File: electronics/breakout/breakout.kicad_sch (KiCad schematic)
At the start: 9 parts, among them J1 2604-3103, J2 2604-3103, J3 2604-3103, J4 2604-3103, J5 2604-3103, J6 2604-3103, J7 2604-3103, J8 2604-3105, J9 2604-3103

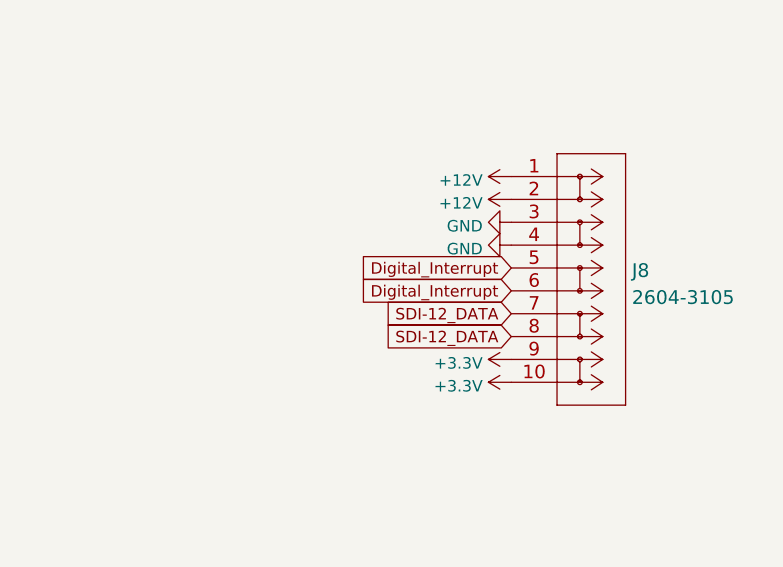
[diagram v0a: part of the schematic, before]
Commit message: Breakout board main connector now in same order as on the Wombat board.
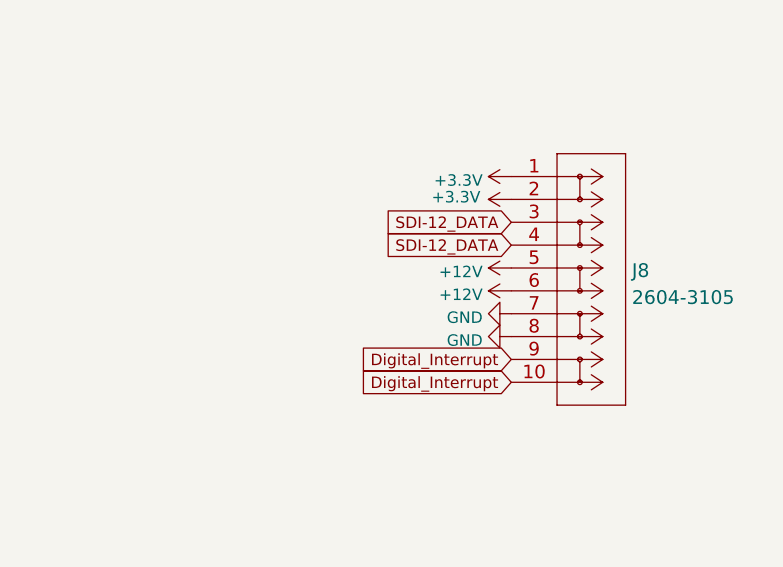
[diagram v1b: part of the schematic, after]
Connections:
- net +12V: now also J8.5, J8.6; no longer J8.1, J8.2
- net +3.3V: now also J8.1, J8.2; no longer J8.10, J8.9
- net Digital_Interrupt: now also J8.10, J8.9; no longer J8.5, J8.6
- net GND: now also J8.7, J8.8; no longer J8.3, J8.4
- net SDI-12_DATA: now also J8.3, J8.4; no longer J8.7, J8.8
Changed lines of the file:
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@@
     )
   )
-  (global_label "SDI-12_DATA" (shape input) (at 205.994 92.964 180) (fields_autoplaced)
-    (effects (font (size 1.27 1.27)) (justify right))
-    (property "Intersheet References" "${INTERSHEET_REFS}" (id 0) (at 191.1228 92.8846 0)
+  (global_label "SDI-12_DATA" (shape input) (at 205.994 82.804 180) (fields_autoplaced)
+    (effects (font (size 1.27 1.27)) (justify right))
+    (property "Intersheet References" "${INTERSHEET_REFS}" (id 0) (at 191.1228 82.7246 0)
       (effects (font (size 1.27 1.27)) (justify right) hide)
     )
@@
     )
   )
-  (global_label "Digital_Interrupt" (shape input) (at 205.994 85.344 180) (fields_autoplaced)
-    (effects (font (size 1.27 1.27)) (justify right))
-    (property "Intersheet References" "${INTERSHEET_REFS}" (id 0) (at 188.2804 85.2646 0)
+  (global_label "Digital_Interrupt" (shape input) (at 205.994 95.504 180) (fields_autoplaced)
+    (effects (font (size 1.27 1.27)) (justify right))
+    (property "Intersheet References" "${INTERSHEET_REFS}" (id 0) (at 188.2804 95.4246 0)
       (effects (font (size 1.27 1.27)) (justify right) hide)
     )
@@
     )
   )
-  (global_label "SDI-12_DATA" (shape input) (at 205.994 90.424 180) (fields_autoplaced)
-    (effects (font (size 1.27 1.27)) (justify right))
-    (property "Intersheet References" "${INTERSHEET_REFS}" (id 0) (at 191.1228 90.3446 0)
+  (global_label "SDI-12_DATA" (shape input) (at 205.994 80.264 180) (fields_autoplaced)
+    (effects (font (size 1.27 1.27)) (justify right))
+    (property "Intersheet References" "${INTERSHEET_REFS}" (id 0) (at 191.1228 80.1846 0)
       (effects (font (size 1.27 1.27)) (justify right) hide)
     )
@@
     )
   )
-  (global_label "Digital_Interrupt" (shape input) (at 205.994 87.884 180) (fields_autoplaced)
-    (effects (font (size 1.27 1.27)) (justify right))
-    (property "Intersheet References" "${INTERSHEET_REFS}" (id 0) (at 188.2804 87.8046 0)
+  (global_label "Digital_Interrupt" (shape input) (at 205.994 98.044 180) (fields_autoplaced)
+    (effects (font (size 1.27 1.27)) (justify right))
+    (property "Intersheet References" "${INTERSHEET_REFS}" (id 0) (at 188.2804 97.9646 0)
       (effects (font (size 1.27 1.27)) (justify right) hide)
     )
@@
     (pin "1")
   )
-  (symbol (lib_id "power:GND") (at 205.994 82.804 270) (unit 1)
-    (in_bom yes) (on_board yes) (fields_autoplaced)
-    (property "Reference" "#PWR032" (id 0) (at 199.644 82.804 0)
-      (effects (font (size 1.27 1.27)) hide)
-    )
-    (property "Value" "GND" (id 1) (at 202.8191 83.2378 90)
-      (effects (font (size 1.27 1.27)) (justify right))
-    )
-    (property "Footprint" "" (id 2) (at 205.994 82.804 0)
-      (effects (font (size 1.27 1.27)) hide)
-    )
-    (property "Datasheet" "" (id 3) (at 205.994 82.804 0)
+  (symbol (lib_id "power:GND") (at 205.994 92.964 270) (unit 1)
+    (in_bom yes) (on_board yes) (fields_autoplaced)
+    (property "Reference" "#PWR032" (id 0) (at 199.644 92.964 0)
+      (effects (font (size 1.27 1.27)) hide)
+    )
+    (property "Value" "GND" (id 1) (at 202.8191 93.3978 90)
+      (effects (font (size 1.27 1.27)) (justify right))
+    )
+    (property "Footprint" "" (id 2) (at 205.994 92.964 0)
+      (effects (font (size 1.27 1.27)) hide)
+    )
+    (property "Datasheet" "" (id 3) (at 205.994 92.964 0)
       (effects (font (size 1.27 1.27)) hide)
     )
@@
     (pin "1")
   )
-  (symbol (lib_id "power:GND") (at 205.994 80.264 270) (unit 1)
-    (in_bom yes) (on_board yes) (fields_autoplaced)
-    (property "Reference" "#PWR031" (id 0) (at 199.644 80.264 0)
-      (effects (font (size 1.27 1.27)) hide)
-    )
-    (property "Value" "GND" (id 1) (at 202.8191 80.6978 90)
-      (effects (font (size 1.27 1.27)) (justify right))
-    )
-    (property "Footprint" "" (id 2) (at 205.994 80.264 0)
-      (effects (font (size 1.27 1.27)) hide)
-    )
-    (property "Datasheet" "" (id 3) (at 205.994 80.264 0)
-      (effects (font (size 1.27 1.27)) hide)
-    )
-    (pin "1")
-  )
-  (symbol (lib_id "power:+3.3V") (at 205.994 98.044 90) (unit 1)
-    (in_bom yes) (on_board yes) (fields_autoplaced)
-    (property "Reference" "#PWR034" (id 0) (at 209.804 98.044 0)
-      (effects (font (size 1.27 1.27)) hide)
-    )
-    (property "Value" "+3.3V" (id 1) (at 202.819 98.4778 90)
-      (effects (font (size 1.27 1.27)) (justify left))
-    )
-    (property "Footprint" "" (id 2) (at 205.994 98.044 0)
-      (effects (font (size 1.27 1.27)) hide)
-    )
-    (property "Datasheet" "" (id 3) (at 205.994 98.044 0)
+  (symbol (lib_id "power:GND") (at 205.994 90.424 270) (unit 1)
+    (in_bom yes) (on_board yes) (fields_autoplaced)
+    (property "Reference" "#PWR031" (id 0) (at 199.644 90.424 0)
+      (effects (font (size 1.27 1.27)) hide)
+    )
+    (property "Value" "GND" (id 1) (at 202.8191 90.8578 90)
+      (effects (font (size 1.27 1.27)) (justify right))
+    )
+    (property "Footprint" "" (id 2) (at 205.994 90.424 0)
+      (effects (font (size 1.27 1.27)) hide)
+    )
+    (property "Datasheet" "" (id 3) (at 205.994 90.424 0)
+      (effects (font (size 1.27 1.27)) hide)
+    )
+    (pin "1")
+  )
+  (symbol (lib_id "power:+3.3V") (at 205.994 77.724 90) (unit 1)
+    (in_bom yes) (on_board yes)
+    (property "Reference" "#PWR034" (id 0) (at 209.804 77.724 0)
+      (effects (font (size 1.27 1.27)) hide)
+    )
+    (property "Value" "+3.3V" (id 1) (at 202.565 77.47 90)
+      (effects (font (size 1.27 1.27)) (justify left))
+    )
+    (property "Footprint" "" (id 2) (at 205.994 77.724 0)
+      (effects (font (size 1.27 1.27)) hide)
+    )
+    (property "Datasheet" "" (id 3) (at 205.994 77.724 0)
       (effects (font (size 1.27 1.27)) hide)
     )
@@
     (pin "1")
   )
-  (symbol (lib_id "power:+12V") (at 205.994 75.184 90) (unit 1)
-    (in_bom yes) (on_board yes) (fields_autoplaced)
-    (property "Reference" "#PWR029" (id 0) (at 209.804 75.184 0)
-      (effects (font (size 1.27 1.27)) hide)
-    )
-    (property "Value" "+12V" (id 1) (at 202.819 75.6178 90)
-      (effects (font (size 1.27 1.27)) (justify left))
-    )
-    (property "Footprint" "" (id 2) (at 205.994 75.184 0)
-      (effects (font (size 1.27 1.27)) hide)
-    )
-    (property "Datasheet" "" (id 3) (at 205.994 75.184 0)
+  (symbol (lib_id "power:+12V") (at 205.994 87.884 90) (unit 1)
+    (in_bom yes) (on_board yes) (fields_autoplaced)
+    (property "Reference" "#PWR029" (id 0) (at 209.804 87.884 0)
+      (effects (font (size 1.27 1.27)) hide)
+    )
+    (property "Value" "+12V" (id 1) (at 202.819 88.3178 90)
+      (effects (font (size 1.27 1.27)) (justify left))
+    )
+    (property "Footprint" "" (id 2) (at 205.994 87.884 0)
+      (effects (font (size 1.27 1.27)) hide)
+    )
+    (property "Datasheet" "" (id 3) (at 205.994 87.884 0)
       (effects (font (size 1.27 1.27)) hide)
     )
@@
     (pin "1")
   )
-  (symbol (lib_id "power:+12V") (at 205.994 77.724 90) (unit 1)
-    (in_bom yes) (on_board yes) (fields_autoplaced)
-    (property "Reference" "#PWR030" (id 0) (at 209.804 77.724 0)
-      (effects (font (size 1.27 1.27)) hide)
-    )
-    (property "Value" "+12V" (id 1) (at 202.819 78.1578 90)
-      (effects (font (size 1.27 1.27)) (justify left))
-    )
-    (property "Footprint" "" (id 2) (at 205.994 77.724 0)
-      (effects (font (size 1.27 1.27)) hide)
-    )
-    (property "Datasheet" "" (id 3) (at 205.994 77.724 0)
+  (symbol (lib_id "power:+12V") (at 205.994 85.344 90) (unit 1)
+    (in_bom yes) (on_board yes) (fields_autoplaced)
+    (property "Reference" "#PWR030" (id 0) (at 209.804 85.344 0)
+      (effects (font (size 1.27 1.27)) hide)
+    )
+    (property "Value" "+12V" (id 1) (at 202.819 85.7778 90)
+      (effects (font (size 1.27 1.27)) (justify left))
+    )
+    (property "Footprint" "" (id 2) (at 205.994 85.344 0)
+      (effects (font (size 1.27 1.27)) hide)
+    )
+    (property "Datasheet" "" (id 3) (at 205.994 85.344 0)
       (effects (font (size 1.27 1.27)) hide)
     )
@@
     (pin "1")
   )
-  (symbol (lib_id "power:+3.3V") (at 205.994 95.504 90) (unit 1)
-    (in_bom yes) (on_board yes) (fields_autoplaced)
-    (property "Reference" "#PWR033" (id 0) (at 209.804 95.504 0)
-      (effects (font (size 1.27 1.27)) hide)
-    )
-    (property "Value" "+3.3V" (id 1) (at 202.819 95.9378 90)
-      (effects (font (size 1.27 1.27)) (justify left))
-    )
-    (property "Footprint" "" (id 2) (at 205.994 95.504 0)
-      (effects (font (size 1.27 1.27)) hide)
-    )
-    (property "Datasheet" "" (id 3) (at 205.994 95.504 0)
-      (effects (font (size 1.27 1.27)) hide)
-    )
+  (symbol (lib_id "power:+3.3V") (at 205.994 75.184 90) (unit 1)
+    (in_bom yes) (on_board yes) (fields_autoplaced)
+    (property "Reference" "#PWR033" (id 0) (at 209.804 75.184 0)
+      (effects (font (size 1.27 1.27)) hide)
+    )
+    (property "Value" "+3.3V" (id 1) (at 202.819 75.6178 90)
+      (effects (font (size 1.27 1.27)) (justify left))
+    )
+    (property "Footprint" "" (id 2) (at 205.994 75.184 0)
+      (effects (font (size 1.27 1.27)) hide)
+    )
+    (property "Datasheet" "" (id 3) (at 205.994 75.184 0)
+      (effects (font (size 1.27 1.27)) hide)
+    )
